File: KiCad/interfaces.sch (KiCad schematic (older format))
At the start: 25 parts, among them J10 5-2337992-8, J2 DF17(4.0)-50DS-0.5V(57), J8 1-2199230-6

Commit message: Loclib
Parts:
- J10: footprint antmicro-footprints:5-2337992-8 -> jetson-nano-baseboard-footprints:5-2337992-8; symbol antmicroModularConnectorsJacksWithMagnetics:5-2337992-8 -> jetson-nano-baseboard:5-2337992-8
- J2: footprint antmicro-footprints:HRS_DF17(4.0)-50DS-0.5V(57) -> jetson-nano-baseboard-footprints:HRS_DF17(4.0)-50DS-0.5V(57); symbol antmicroRectangularConnectorsHeadersMalePins:DF17(4.0)-50DS-0.5V(57) -> jetson-nano-baseboard:DF17(4.0)-50DS-0.5V(57)
- J8: footprint antmicro-footprints:1-2199230-6 -> jetson-nano-baseboard-footprints:1-2199230-6; symbol antmicroPciConnectors:1-2199230-6 -> jetson-nano-baseboard:1-2199230-6
- SP7: footprint antmicro-footprints:9774025151 -> jetson-nano-baseboard-footprints:9774025151; symbol antmicroMechanicalParts:9774025151 -> jetson-nano-baseboard:9774025151
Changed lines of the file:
@@
 	7600 7800 8400 7800
 $Comp
-L antmicroPciConnectors:1-2199230-6 J8
+L jetson-nano-baseboard:1-2199230-6 J8
 U 1 1 6246454E
 P 5475 7150
 F 0 "J8" H 5475 9815 60  0000 C CNN
 F 1 "1-2199230-6" H 5325 5450 60  0001 C CNN
-F 2 "antmicro-footprints:1-2199230-6" H 5325 5450 60  0001 C CNN
+F 2 "jetson-nano-baseboard-footprints:1-2199230-6" H 5325 5450 60  0001 C CNN
 F 3 "" H 5325 7150 60  0001 C CNN
 F 4 "TE" H 5475 9717 50  0000 C CNN "Manufacturer"
@@
 $EndComp
 $Comp
-L antmicroMechanicalParts:9774025151 SP7
+L jetson-nano-baseboard:9774025151 SP7
 U 1 1 6248F20F
 P 5500 9300
 F 0 "SP7" H 5443 9011 60  0000 C CNN
 F 1 "9774025151" H 5443 9117 60  0000 C CNN
-F 2 "antmicro-footprints:9774025151" H 5500 9300 60  0001 C CNN
+F 2 "jetson-nano-baseboard-footprints:9774025151" H 5500 9300 60  0001 C CNN
 F 3 "" H 5500 9300 60  0001 C CNN
 F 4 "Wurth Elektronik" H 5500 9300 50  0001 C CNN "Manufacturer"
@@
 $EndComp
 $Comp
-L antmicroRectangularConnectorsHeadersMalePins:DF17(4.0)-50DS-0.5V(57) J2
+L jetson-nano-baseboard:DF17(4.0)-50DS-0.5V(57) J2
 U 1 1 6211ADC9
 P 10400 2275
 F 0 "J2" H 10400 3742 50  0000 C CNN
 F 1 "DF17(4.0)-50DS-0.5V(57)" H 10400 3651 50  0000 C CNN
-F 2 "antmicro-footprints:HRS_DF17(4.0)-50DS-0.5V(57)" H 10400 675 50  0001 C CNN
+F 2 "jetson-nano-baseboard-footprints:HRS_DF17(4.0)-50DS-0.5V(57)" H 10400 675 50  0001 C CNN
 F 3 "https://www.hirose.com/product/p/CL0683-0045-5-57" H 10500 1075 50  0001 L BNN
 F 4 "HRS" H 10400 775 50  0001 C CNN "Manufacturer"
@@
 	13225 6400 13825 6400
 $Comp
-L antmicroModularConnectorsJacksWithMagnetics:5-2337992-8 J10
+L jetson-nano-baseboard:5-2337992-8 J10
 U 1 1 628CFF58
 P 13325 4975
 F 0 "J10" H 15325 5396 60  0000 C CNN
 F 1 "5-2337992-8" H 15325 5290 60  0000 C CNN
-F 2 "antmicro-footprints:5-2337992-8" H 15325 2925 60  0001 C CNN
+F 2 "jetson-nano-baseboard-footprints:5-2337992-8" H 15325 2925 60  0001 C CNN
 F 3 "" H 14775 4825 60  0000 C CNN
 F 4 "5-2337992-8" H 15325 5192 50  0000 C CNN "MPN"

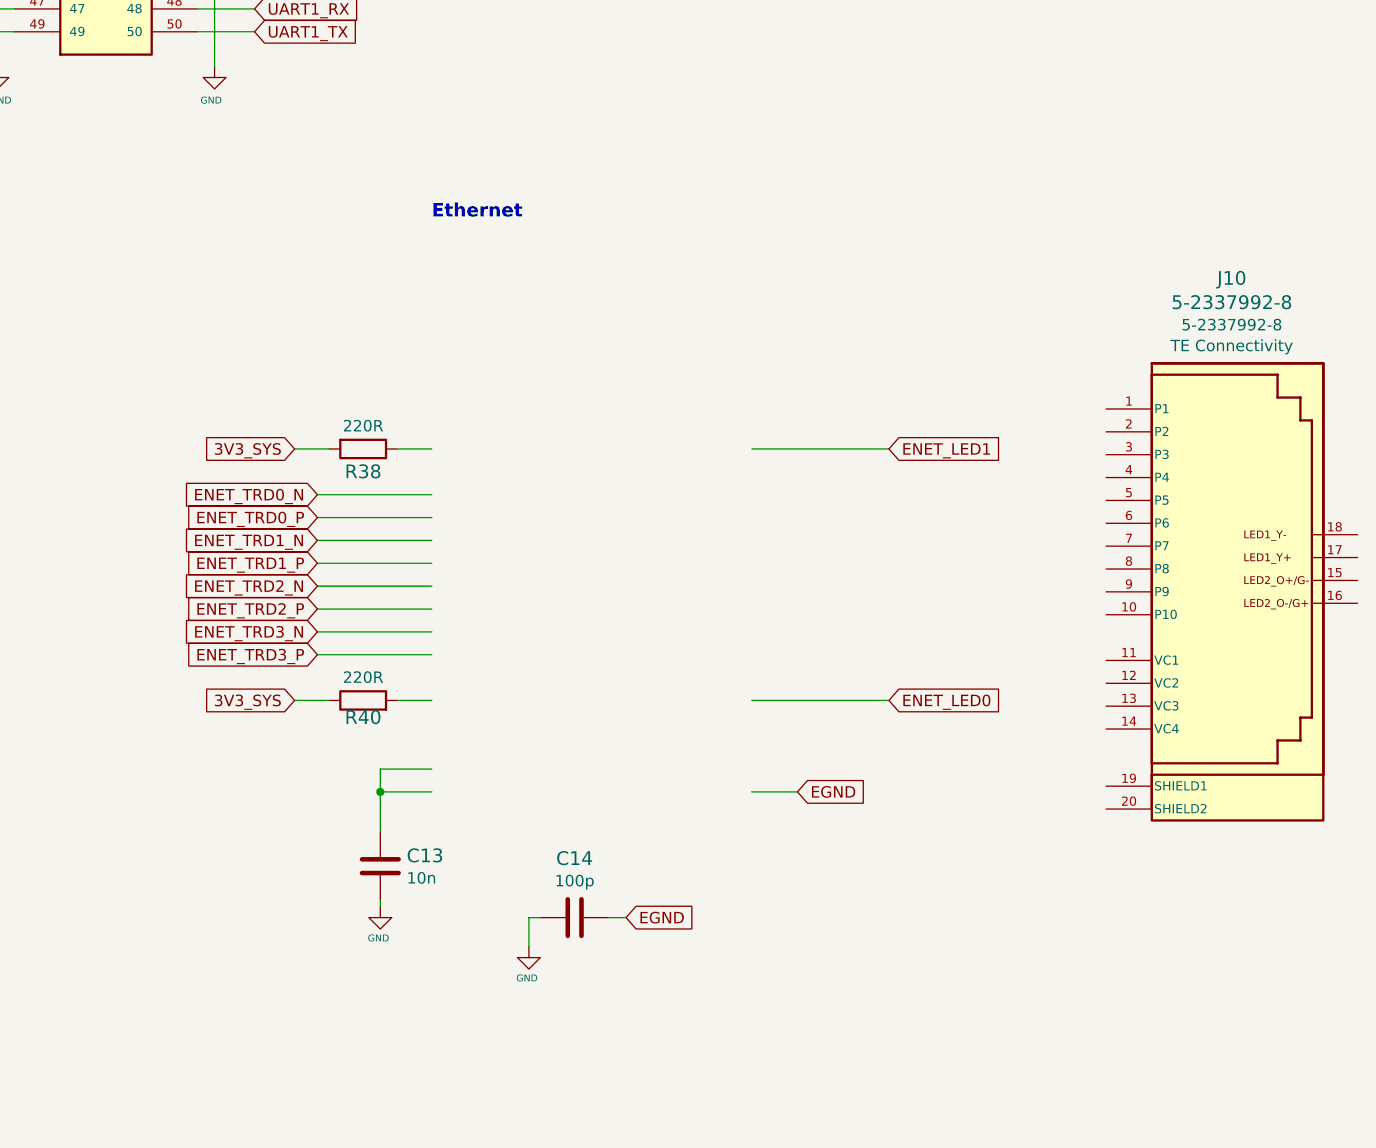
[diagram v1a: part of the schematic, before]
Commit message: Connect OTG USB and Ethernet on schematic
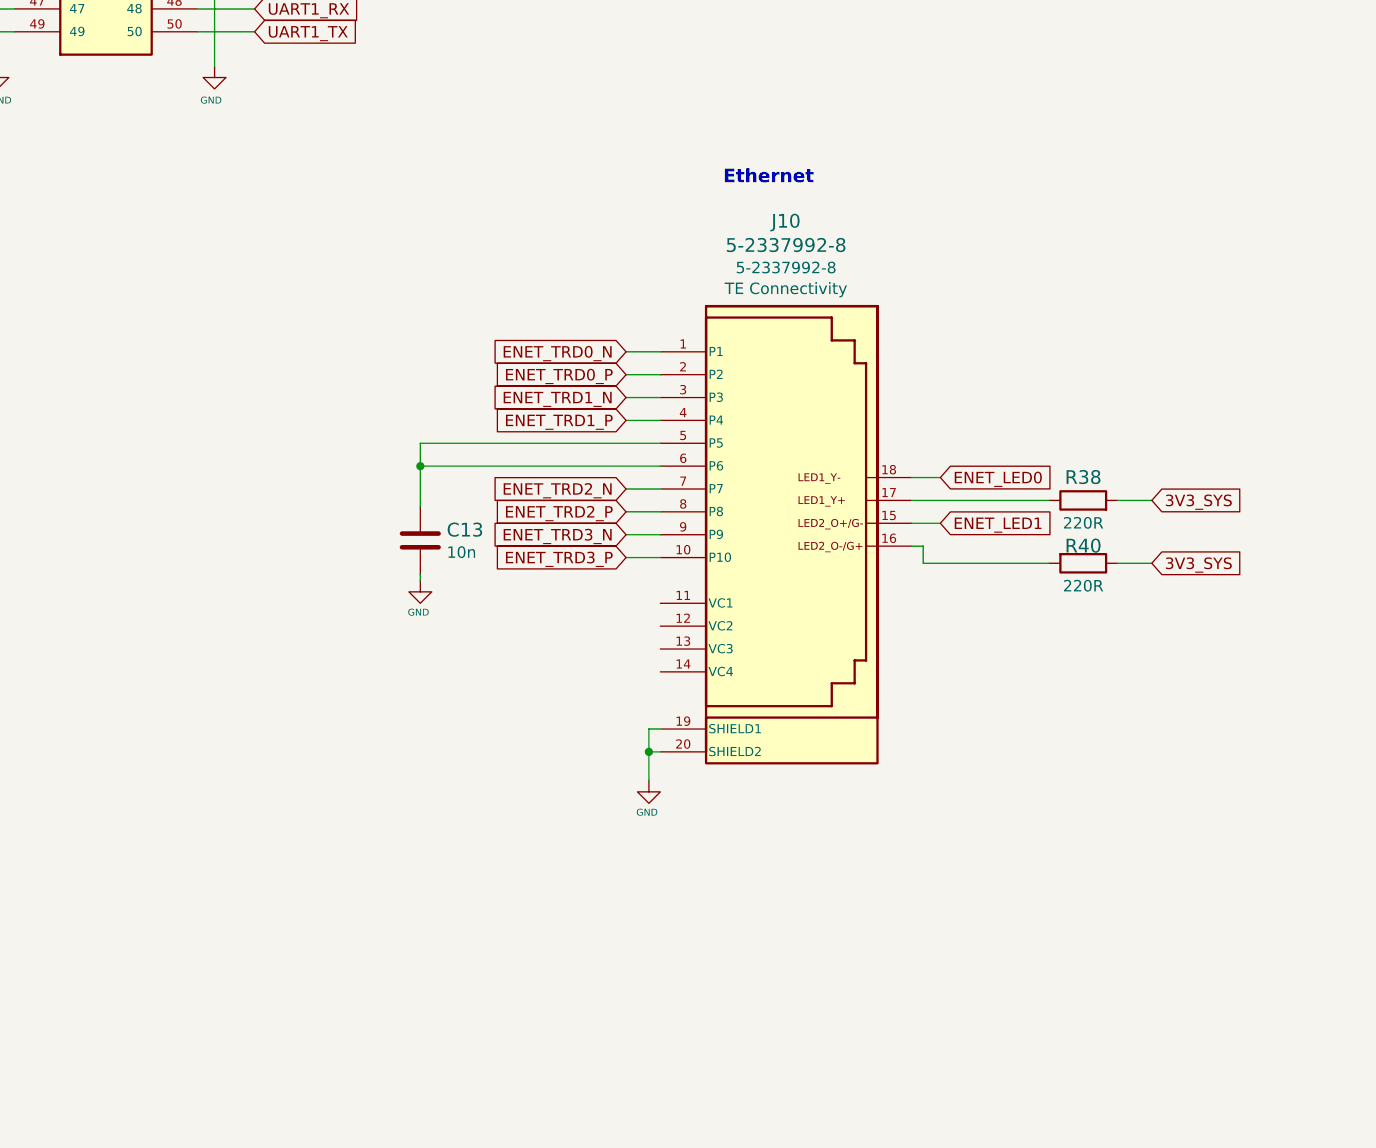
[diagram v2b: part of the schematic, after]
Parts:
- removed C14: C_100p_0402, jetson-nano-baseboard-footprints:0402-cap, symbol jetson-nano-baseboard:C_100p_0402
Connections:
- net labels removed: EGND
- wire segments 195 -> 197
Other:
- moved on the sheet: C13, J10, R38, R40
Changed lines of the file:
@@
 Text Notes 2669 49363 0    60   ~ 0
 Text
-Text Notes 11825 4300 0    59   ~ 12
+Text Notes 13100 4150 0    59   ~ 12
 Ethernet
 Text Notes 4783 4310 0    59   ~ 12
@@
 VIN
 Wire Wire Line
-	12300 7350 12250 7350
-Wire Wire Line
-	12600 7350 12675 7350
-$Comp
-L jetson-nano-baseboard:C_100p_0402 C14
-U 1 1 62BE91A7
-P 12450 7350
-F 0 "C14" V 12192 7350 60  0000 C CNN
-F 1 "C_100p_0402" H 12450 7200 60  0001 C CNN
-F 2 "jetson-nano-baseboard-footprints:0402-cap" H 12650 7550 60  0001 L CNN
-F 3 "" H 12450 7350 50  0001 C CNN
-F 4 "WALSIN" H 12650 7750 60  0001 L CNN "Manufacturer"
-F 5 "0402N101J500CT" H 12650 7650 60  0001 L CNN "MPN"
-F 6 "100p" V 12290 7350 50  0000 C CNN "Val"
-	1    12450 7350
-	0    1    1    0
-$EndComp
-Wire Wire Line
-	12250 7350 12250 7475
+	12825 6625 12775 6625
+Wire Wire Line
+	12775 6625 12775 6750
 $Comp
 L jetson-nano-baseboard:GND #GND_037
 U 1 1 5E710452
-P 12250 7475
-F 0 "#GND_037" H 12250 7475 20  0001 C CNN
-F 1 "GND" H 12242 7335 30  0000 C CNN
-F 2 "" H 12250 7475 70  0001 C CNN
-F 3 "" H 12250 7475 70  0001 C CNN
-	1    12250 7475
-	1    0    0    -1
-$EndComp
-Text GLabel 12675 7350 2    50   Input ~ 0
-EGND
-Wire Wire Line
-	13225 6800 13425 6800
-Text GLabel 13425 6800 2    50   Input ~ 0
-EGND
-Wire Wire Line
-	11600 7275 11600 7300
-Wire Wire Line
-	11600 6800 11600 6975
+P 12775 6750
+F 0 "#GND_037" H 12775 6750 20  0001 C CNN
+F 1 "GND" H 12767 6610 30  0000 C CNN
+F 2 "" H 12775 6750 70  0001 C CNN
+F 3 "" H 12775 6750 70  0001 C CNN
+	1    12775 6750
+	1    0    0    -1
+$EndComp
+Wire Wire Line
+	11775 5850 11775 5875
+Wire Wire Line
+	11775 5375 11775 5550
 $Comp
 L jetson-nano-baseboard:C_10n_0402 C13
 U 1 1 62BF5934
-P 11600 7125
-F 0 "C13" H 11715 7170 60  0000 L CNN
-F 1 "C_10n_0402" H 11600 6975 60  0001 C CNN
-F 2 "jetson-nano-baseboard-footprints:0402-cap" H 11800 7325 60  0001 L CNN
-F 3 "" H 11600 7125 50  0001 C CNN
-F 4 "AVX" H 11800 7525 60  0001 L CNN "Manufacturer"
-F 5 "04025G103ZAT2A" H 11800 7425 60  0001 L CNN "MPN"
-F 6 "10n" H 11715 7072 50  0000 L CNN "Val"
-	1    11600 7125
-	1    0    0    -1
-$EndComp
-Connection ~ 11600 6800
-Wire Wire Line
-	11825 6800 11600 6800
-Wire Wire Line
-	11600 6700 11600 6800
-Wire Wire Line
-	11825 6700 11600 6700
+P 11775 5700
+F 0 "C13" H 11890 5745 60  0000 L CNN
+F 1 "C_10n_0402" H 11775 5550 60  0001 C CNN
+F 2 "jetson-nano-baseboard-footprints:0402-cap" H 11975 5900 60  0001 L CNN
+F 3 "" H 11775 5700 50  0001 C CNN
+F 4 "AVX" H 11975 6100 60  0001 L CNN "Manufacturer"
+F 5 "04025G103ZAT2A" H 11975 6000 60  0001 L CNN "MPN"
+F 6 "10n" H 11890 5647 50  0000 L CNN "Val"
+	1    11775 5700
+	1    0    0    -1
+$EndComp
+Connection ~ 11775 5375
+Wire Wire Line
+	11775 5275 11775 5375
 $Comp
 L jetson-nano-baseboard:GND #GND_036
 U 1 1 5E710455
-P 11600 7300
-F 0 "#GND_036" H 11600 7300 20  0001 C CNN
-F 1 "GND" H 11592 7160 30  0000 C CNN
-F 2 "" H 11600 7300 70  0001 C CNN
-F 3 "" H 11600 7300 70  0001 C CNN
-	1    11600 7300
-	1    0    0    -1
-$EndComp
-Text GLabel 11325 6200 0    50   Input ~ 0
+P 11775 5875
+F 0 "#GND_036" H 11775 5875 20  0001 C CNN
+F 1 "GND" H 11767 5735 30  0000 C CNN
+F 2 "" H 11775 5875 70  0001 C CNN
+F 3 "" H 11775 5875 70  0001 C CNN
+	1    11775 5875
+	1    0    0    -1
+$EndComp
+Text GLabel 12675 5775 0    50   Input ~ 0
 ENET_TRD3_P
-Text GLabel 11325 6100 0    50   Input ~ 0
+Text GLabel 12675 5675 0    50   Input ~ 0
 ENET_TRD3_N
-Text GLabel 11325 6000 0    50   Input ~ 0
+Text GLabel 12675 5575 0    50   Input ~ 0
 ENET_TRD2_P
-Text GLabel 11325 5900 0    50   Input ~ 0
+Text GLabel 12675 5475 0    50   Input ~ 0
 ENET_TRD2_N
-Text GLabel 11325 5800 0    50   Input ~ 0
+Text GLabel 12675 5175 0    50   Input ~ 0
 ENET_TRD1_P
-Text GLabel 11325 5700 0    50   Input ~ 0
+Text GLabel 12675 5075 0    50   Input ~ 0
 ENET_TRD1_N
-Text GLabel 11325 5600 0    50   Input ~ 0
+Text GLabel 12675 4975 0    50   Input ~ 0
 ENET_TRD0_P
-Text GLabel 11325 5500 0    50   Input ~ 0
+Text GLabel 12675 4875 0    50   Input ~ 0
 ENET_TRD0_N
 Wire Wire Line
-	11325 6200 11825 6200
-Wire Wire Line
-	11325 6100 11825 6100
-Wire Wire Line
-	11325 6000 11825 6000
-Wire Wire Line
-	11325 5900 11825 5900
-Wire Wire Line
-	11325 5800 11825 5800
-Wire Wire Line
-	11325 5700 11825 5700
-Wire Wire Line
-	11825 5600 11325 5600
-Wire Wire Line
-	11825 5500 11325 5500
-Wire Wire Line
-	11825 6400 11675 6400
-Wire Wire Line
-	11375 6400 11225 6400
+	12675 5775 12825 5775
+Wire Wire Line
+	12675 5675 12825 5675
+Wire Wire Line
+	12675 5575 12825 5575
+Wire Wire Line
+	12675 5475 12825 5475
+Wire Wire Line
+	12675 5175 12825 5175
+Wire Wire Line
+	12675 5075 12825 5075
+Wire Wire Line
+	12825 4975 12675 4975
+Wire Wire Line
+	12825 4875 12675 4875
+Wire Wire Line
+	14825 5800 14975 5800
 $Comp
 L jetson-nano-baseboard:R_220R_0402 R40
 U 1 1 62BCA909
-P 11525 6400
-F 0 "R40" H 11525 6325 60  0000 C CNN
-F 1 "R_220R_0402" H 11525 6250 60  0001 C CNN
-F 2 "jetson-nano-baseboard-footprints:0402-res" H 11725 6600 60  0001 L CNN
-F 3 "" H 11525 6400 50  0001 C CNN
-F 4 "Panasonic" H 11725 6800 60  0001 L CNN "Manufacturer"
-F 5 "ERJ2GEJ221X" H 11725 6700 60  0001 L CNN "MPN"
-F 6 "220R" H 11525 6500 50  0000 C CNN "Val"
-	1    11525 6400
-	1    0    0    -1
-$EndComp
-Text GLabel 11225 6400 0    50   Input ~ 0
+P 14675 5800
+F 0 "R40" H 14675 5725 60  0000 C CNN
+F 1 "R_220R_0402" H 14675 5650 60  0001 C CNN
+F 2 "jetson-nano-baseboard-footprints:0402-res" H 14875 6000 60  0001 L CNN
+F 3 "" H 14675 5800 50  0001 C CNN
+F 4 "Panasonic" H 14875 6200 60  0001 L CNN "Manufacturer"
+F 5 "ERJ2GEJ221X" H 14875 6100 60  0001 L CNN "MPN"
+F 6 "220R" H 14675 5900 50  0000 C CNN "Val"
+	1    14675 5800
+	-1   0    0    1
+$EndComp
+Text GLabel 14975 5800 2    50   Input ~ 0
 3V3_SYS
-Text GLabel 11225 5300 0    50   Input ~ 0
+Text GLabel 14975 5525 2    50   Input ~ 0
 3V3_SYS
 $Comp
 L jetson-nano-baseboard:R_220R_0402 R38
 U 1 1 62BC9C4E
-P 11525 5300
-F 0 "R38" H 11525 5400 60  0000 C CNN
-F 1 "R_220R_0402" H 11525 5150 60  0001 C CNN
-F 2 "jetson-nano-baseboard-footprints:0402-res" H 11725 5500 60  0001 L CNN
-F 3 "" H 11525 5300 50  0001 C CNN
-F 4 "Panasonic" H 11725 5700 60  0001 L CNN "Manufacturer"
-F 5 "ERJ2GEJ221X" H 11725 5600 60  0001 L CNN "MPN"
-F 6 "220R" H 11525 5200 50  0000 C CNN "Val"
-	1    11525 5300
-	-1   0    0    1
-$EndComp
-Wire Wire Line
-	11375 5300 11225 5300
-Wire Wire Line
-	11825 5300 11675 5300
-Text GLabel 13825 6400 2    50   Input ~ 0
+P 14675 5525
+F 0 "R38" H 14675 5625 60  0000 C CNN
+F 1 "R_220R_0402" H 14675 5375 60  0001 C CNN
+F 2 "jetson-nano-baseboard-footprints:0402-res" H 14875 5725 60  0001 L CNN
+F 3 "" H 14675 5525 50  0001 C CNN
+F 4 "Panasonic" H 14875 5925 60  0001 L CNN "Manufacturer"
+F 5 "ERJ2GEJ221X" H 14875 5825 60  0001 L CNN "MPN"
+F 6 "220R" H 14675 5425 50  0000 C CNN "Val"
+	1    14675 5525
+	1    0    0    -1
+$EndComp
+Wire Wire Line
+	14825 5525 14975 5525
+Text GLabel 14050 5425 2    50   Input ~ 0
 ENET_LED0
-Text GLabel 13825 5300 2    50   Input ~ 0
+Text GLabel 14050 5625 2    50   Input ~ 0
 ENET_LED1
 Wire Wire Line
-	13225 5300 13825 5300
-Wire Wire Line
-	13225 6400 13825 6400
+	13925 5625 14050 5625
+Wire Wire Line
+	13925 5425 14050 5425
+Wire Wire Line
+	11775 5275 12825 5275
+Wire Wire Line
+	11775 5375 12825 5375
+Wire Wire Line
+	12825 6525 12775 6525
+Wire Wire Line
+	12775 6525 12775 6625
+Connection ~ 12775 6625
+Wire Wire Line
+	13925 5525 14525 5525
+Wire Wire Line
+	13975 5800 13975 5725
+Wire Wire Line
+	13975 5725 13925 5725
+Wire Wire Line
+	13975 5800 14525 5800
 $Comp
 L jetson-nano-baseboard:5-2337992-8 J10
 U 1 1 628CFF58
-P 13325 4975
-F 0 "J10" H 15325 5396 60  0000 C CNN
-F 1 "5-2337992-8" H 15325 5290 60  0000 C CNN
-F 2 "jetson-nano-baseboard-footprints:5-2337992-8" H 15325 2925 60  0001 C CNN
-F 3 "" H 14775 4825 60  0000 C CNN
-F 4 "5-2337992-8" H 15325 5192 50  0000 C CNN "MPN"
-F 5 "TE Connectivity" H 15325 5101 50  0000 C CNN "Manufacturer"
-	1    13325 4975
-	1    0    0    -1
-$EndComp
+P 11375 4725
+F 0 "J10" H 13375 5146 60  0000 C CNN
+F 1 "5-2337992-8" H 13375 5040 60  0000 C CNN
+F 2 "jetson-nano-baseboard-footprints:5-2337992-8" H 13375 2675 60  0001 C CNN
+F 3 "" H 12825 4575 60  0000 C CNN
+F 4 "5-2337992-8" H 13375 4942 50  0000 C CNN "MPN"
+F 5 "TE Connectivity" H 13375 4851 50  0000 C CNN "Manufacturer"
+	1    11375 4725
+	1    0    0    -1
+$EndComp

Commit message: Add b2b connector for POE signals
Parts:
- added J3: 62100421821, jetson-nano-baseboard-footprints:621304242921, symbol jetson-nano-baseboard:62100421821
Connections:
- net labels added: ENET_VC1, ENET_VC2, ENET_VC3, ENET_VC4
- wire segments 197 -> 205
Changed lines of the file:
@@
 	1    0    0    -1
 $EndComp
+$Comp
+L jetson-nano-baseboard:62100421821 J3
+U 1 1 621FE060
+P 11725 6625
+F 0 "J3" H 11725 6816 60  0000 C CNN
+F 1 "62100421821" H 12425 7325 60  0001 C CNN
+F 2 "jetson-nano-baseboard-footprints:621304242921" H 11950 7225 60  0001 L CNN
+F 3 "https://www.we-online.com/catalog/datasheet/62100421821.pdf" V 11925 7175 60  0001 L CNN
+F 4 "62100421821" H 11950 7425 60  0001 L CNN "MPN"
+F 5 "Wurth Elektronik" H 11950 7525 60  0001 L CNN "Manufacturer"
+	1    11725 6625
+	1    0    0    -1
+$EndComp
+Text Label 12675 5975 2    50   ~ 0
+ENET_VC1
+Wire Wire Line
+	12675 5975 12825 5975
+Wire Wire Line
+	12675 6075 12825 6075
+Wire Wire Line
+	12675 6175 12825 6175
+Wire Wire Line
+	12675 6275 12825 6275
+Text Label 12675 6075 2    50   ~ 0
+ENET_VC2
+Text Label 12675 6175 2    50   ~ 0
+ENET_VC3
+Text Label 12675 6275 2    50   ~ 0
+ENET_VC4
+Text Label 11375 6575 2    50   ~ 0
+ENET_VC1
+Wire Wire Line
+	11375 6575 11525 6575
+Text Label 12075 6575 0    50   ~ 0
+ENET_VC2
+Wire Wire Line
+	11925 6575 12075 6575
+Text Label 11375 6675 2    50   ~ 0
+ENET_VC4
+Wire Wire Line
+	11525 6675 11375 6675
+Wire Wire Line
+	11925 6675 12075 6675
+Text Label 12075 6675 0    50   ~ 0
+ENET_VC3
 $EndSCHEMATC
